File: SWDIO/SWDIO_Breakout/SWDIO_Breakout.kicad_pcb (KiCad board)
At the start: 2 copper layers, 38 x 20 mm, 2 parts, among them J1 8.06.16, J2 Conn_01x05_Male

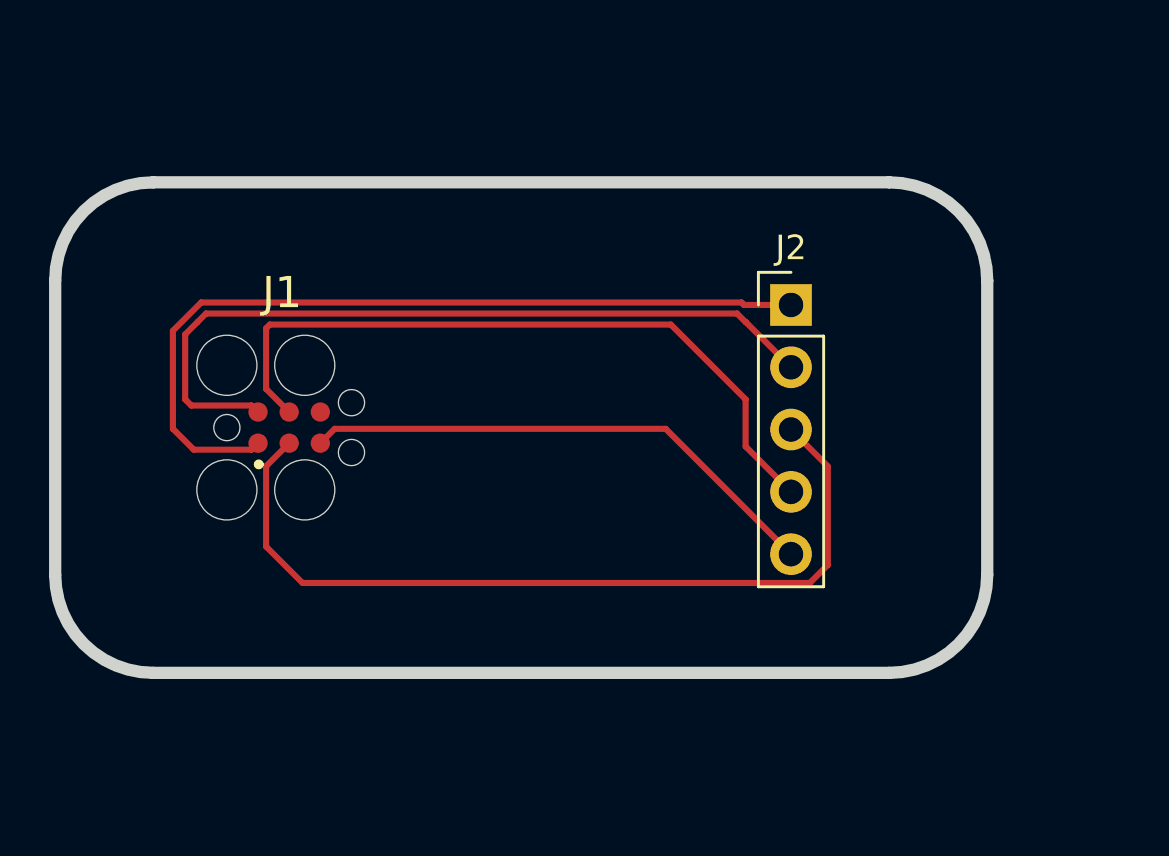
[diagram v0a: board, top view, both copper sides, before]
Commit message: added 20 pin for testing/backup
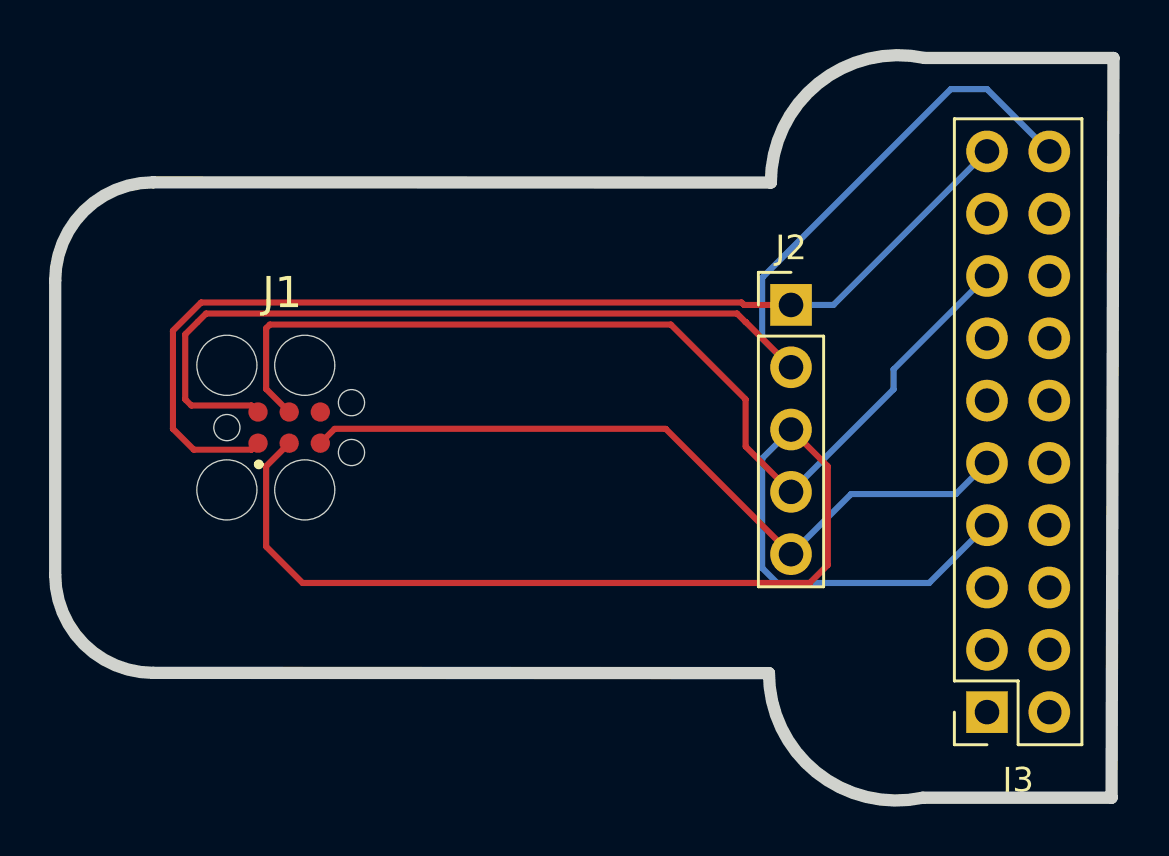
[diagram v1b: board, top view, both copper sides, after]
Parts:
- added J3: Conn_01x20_Male, Connector_PinSocket_2.54mm:PinSocket_2x10_P2.54mm_Vertical, F.Cu at (174.0, 101.6)
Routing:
- net GND: track 31.8 -> 51.9 mm
- net SWDIO: track 34.6 -> 51.1 mm
- net RESET: track 29.2 -> 41.3 mm
- net +3.3V: track 34.0 -> 44.6 mm
- net SWCLK: track 21.5 -> 31.1 mm
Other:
- board size 38 x 20 mm -> 43.1 x 30.4 mm
